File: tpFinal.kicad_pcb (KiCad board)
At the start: 2 copper layers, 50 x 100 mm, 42 parts, among them P1 CONN_UART_TX_RX, P2 CONN_SPK, P3 CONN_PWR, P4 CONN_BAT, P5 CONN_SWD, U1 EMW3166, U2 MCP73831-2-OT, U3 AUR9705AGH, U4 SPH0644HM4H-1, U5 MAX98357A

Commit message: correciones varias según revisiones
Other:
- board text added: "Fabricante: seeedstudio Grillas: 1 mm ,0,5 mm , 0,25 mm Via: 0.8 mm / 0.4 mm Margen: 0.2 mm Pista: 0.6 mm, 0.4 mm, 0,25 mm , 0.2 mm Dist. a borde: 0.80 mm Material: FR-4 TG130 Terminacion: HASL"
- board text removed: "Grillas: 1 mm ,0,5 mm , 0,25 mm Via: 0.8 mm / 0.4 mm Margen: 0.2 mm Pista: 0.6 mm, 0.4 mm, 0,25 mm , 0.2 mm Dist. a borde: 0.80 mm Material: FR-4 TG130 Terminacion: HASL"
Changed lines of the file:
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@@
     (tags resistor)
     (attr smd)
-    (fp_text reference R5 (at 0 -1.65 270) (layer F.SilkS)
+    (fp_text reference R5 (at 2.4375 -0.5) (layer F.SilkS)
       (effects (font (size 1 1) (thickness 0.15)))
     )
@@
     (tags resistor)
     (attr smd)
-    (fp_text reference R6 (at 0 -1.65 270) (layer F.SilkS)
+    (fp_text reference R6 (at 2.4375 -0.5) (layer F.SilkS)
       (effects (font (size 1 1) (thickness 0.15)))
     )
@@
     (tags resistor)
     (attr smd)
-    (fp_text reference R7 (at 0 -1.65 270) (layer F.SilkS)
+    (fp_text reference R7 (at 2.9375 -0.5) (layer F.SilkS)
       (effects (font (size 1 1) (thickness 0.15)))
     )
@@
     (tags resistor)
     (attr smd)
-    (fp_text reference R8 (at 0 -1.65 270) (layer F.SilkS)
+    (fp_text reference R8 (at 2.9375 -0.5 180) (layer F.SilkS)
       (effects (font (size 1 1) (thickness 0.15)))
     )
@@
       (solder_mask_margin 0.5) (clearance 0.5))
   )
-  (gr_text "Grillas: 1 mm ,0,5 mm , 0,25 mm\nVia: 0.8 mm / 0.4 mm\nMargen: 0.2 mm\nPista: 0.6 mm, 0.4 mm, 0,25 mm , 0.2 mm\nDist. a borde: 0.80 mm\nMaterial: FR-4 TG130\nTerminacion: HASL" (at 198 61) (layer Dwgs.User)
+  (gr_text "Fabricante: seeedstudio\nGrillas: 1 mm ,0,5 mm , 0,25 mm\nVia: 0.8 mm / 0.4 mm\nMargen: 0.2 mm\nPista: 0.6 mm, 0.4 mm, 0,25 mm , 0.2 mm\nDist. a borde: 0.80 mm\nMaterial: FR-4 TG130\nTerminacion: HASL" (at 198 61) (layer Dwgs.User)
     (effects (font (size 1.5 1.5) (thickness 0.3)) (justify left))
   )
@@
     (effects (font (size 1.5 1.5) (thickness 0.3)) (justify mirror))
   )
-  (dimension 94 (width 0.3) (layer F.SilkS)
-    (gr_text "94,000 mm" (at 192.1 88 270) (layer F.SilkS)
+  (dimension 94 (width 0.3) (layer Dwgs.User)
+    (gr_text "94,000 mm" (at 192.1 88 270) (layer Dwgs.User)
       (effects (font (size 1.5 1.5) (thickness 0.3)))
     )
@@
     (arrow2b (pts (xy 190 41) (xy 190.586421 42.126504)))
   )
-  (dimension 44 (width 0.3) (layer F.SilkS)
-    (gr_text "44,000 mm" (at 162 142.1) (layer F.SilkS)
+  (dimension 44 (width 0.3) (layer Dwgs.User)
+    (gr_text "44,000 mm" (at 162 142.1) (layer Dwgs.User)
       (effects (font (size 1.5 1.5) (thickness 0.3)))
     )
@@
     (arrow2b (pts (xy 140 140) (xy 141.126504 139.413579)))
   )
-  (dimension 100 (width 0.3) (layer F.SilkS)
-    (gr_text "100,000 mm" (at 196.1 88 270) (layer F.SilkS)
+  (dimension 100 (width 0.3) (layer Dwgs.User)
+    (gr_text "100,000 mm" (at 196.1 88 270) (layer Dwgs.User)
       (effects (font (size 1.5 1.5) (thickness 0.3)))
     )
@@
     (arrow2b (pts (xy 194 38) (xy 194.586421 39.126504)))
   )
-  (dimension 50 (width 0.3) (layer F.SilkS)
-    (gr_text "50,000 mm" (at 162 146.1) (layer F.SilkS)
+  (dimension 50 (width 0.3) (layer Dwgs.User)
+    (gr_text "50,000 mm" (at 162 146.1) (layer Dwgs.User)
       (effects (font (size 1.5 1.5) (thickness 0.3)))
     )

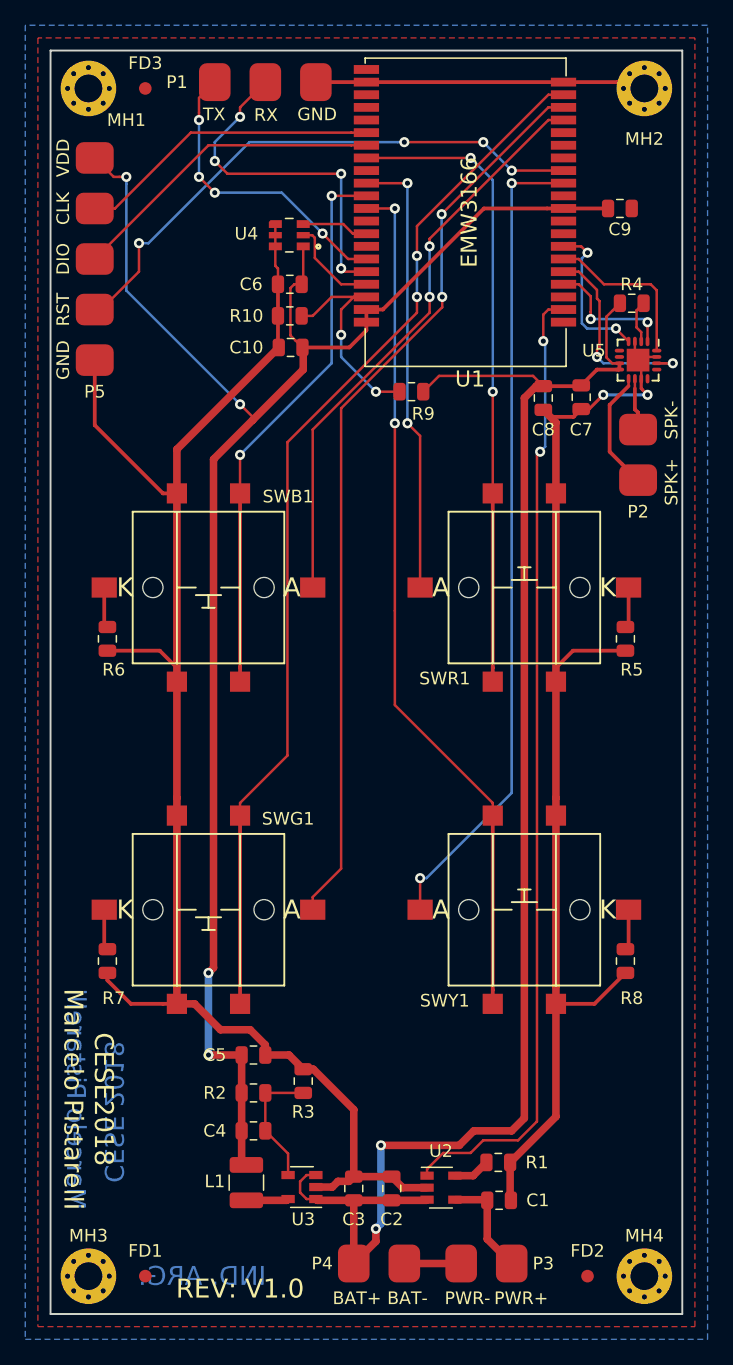
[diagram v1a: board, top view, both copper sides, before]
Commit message: Referencias de fiduciales y agujeros de sujeción configuradas invisibles
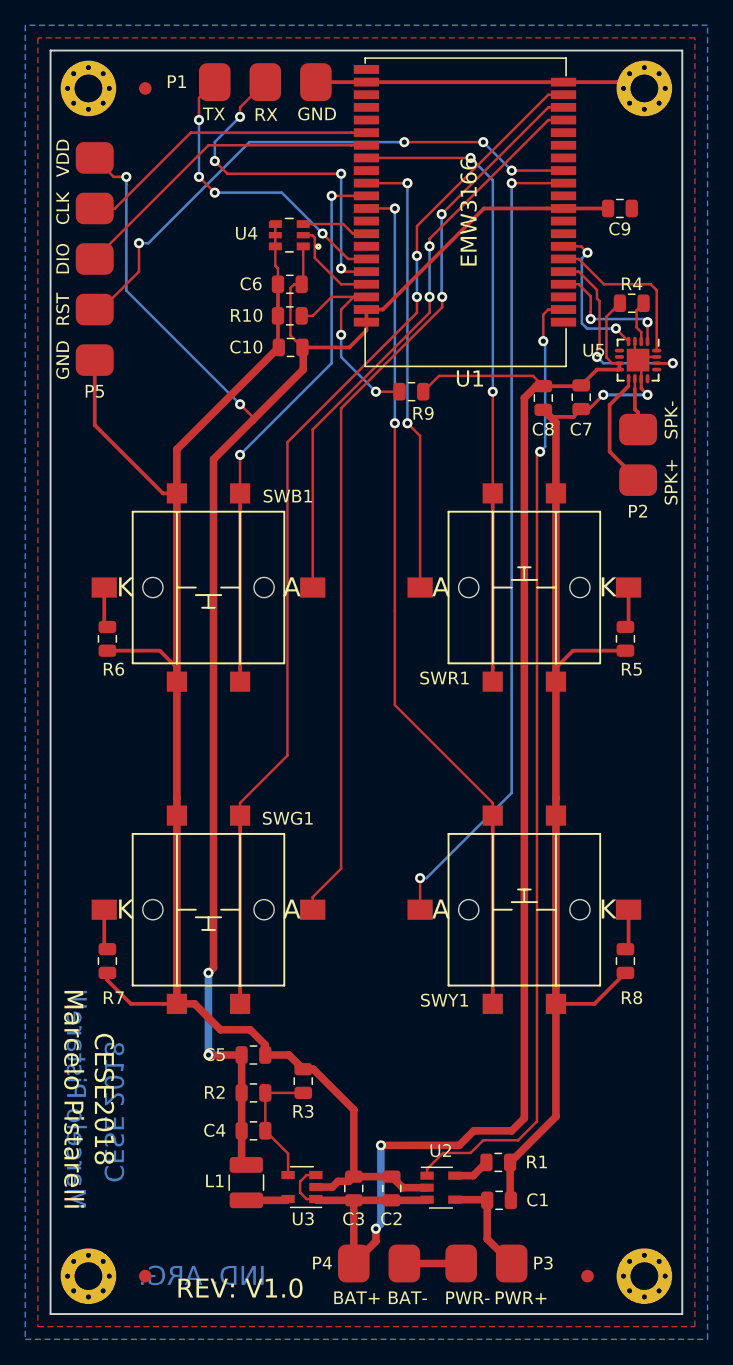
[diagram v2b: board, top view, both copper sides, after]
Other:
- board text added: "Reglas de fabricación de SeeedStudio: 1) https://www.seeedstudio.com/fusion_pcb.html 2) http://support.seeedstudio.com/knowledgebase/articles/447362-fusion-pcb-specification El criterio de selección de ancho mínimo de pista de 6/6 mil es conforme a las capacidades de fabricación de SeeedStudio. Donde 6/6 mil es la tecnología más económica que ofrece, también soporta a un mayor precio las tecnolog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"
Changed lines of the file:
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@@
-(kicad_pcb (version 20171130) (host pcbnew 5.0.0-fee4fd1~66~ubuntu16.04.1)
+(kicad_pcb (version 20171130) (host pcbnew 5.0.1-33cea8e~67~ubuntu16.04.1)
   (general
     (thickness 1.6)
-    (drawings 14)
+    (drawings 15)
     (tracks 398)
     (zones 0)
@@
     (date 2018-10-18)
     (rev 1.0)
-    (company "Marcelo Pistarelli")
+    (company "Empresa: Marcelo Pistarelli")
+    (comment 1 "Creative Commons - Attribution - ShareAlike 3.0")
   )
   (layers
@@
     (pad_drill 0.762)
     (pad_to_mask_clearance 0.2)
+    (solder_mask_min_width 0.25)
     (aux_axis_origin 0 0)
     (visible_elements FFFFFF7F)
@@
     (tags "mounting hole 2.2mm m2")
     (attr virtual)
-    (fp_text reference MH1 (at 3 2.5) (layer F.SilkS)
+    (fp_text reference MH1 (at 3 2.5) (layer F.SilkS) hide
       (effects (font (size 1 1) (thickness 0.15)))
     )
@@
     (tags "mounting hole 2.2mm m2")
     (attr virtual)
-    (fp_text reference MH2 (at 0 4) (layer F.SilkS)
+    (fp_text reference MH2 (at 0 4) (layer F.SilkS) hide
       (effects (font (size 1 1) (thickness 0.15)))
     )
@@
     (tags "mounting hole 2.2mm m2")
     (attr virtual)
-    (fp_text reference MH3 (at 0 -3.2) (layer F.SilkS)
+    (fp_text reference MH3 (at 0 -3.2) (layer F.SilkS) hide
       (effects (font (size 1 1) (thickness 0.15)))
     )
@@
     (tags "mounting hole 2.2mm m2")
     (attr virtual)
-    (fp_text reference MH4 (at 0 -3.2) (layer F.SilkS)
+    (fp_text reference MH4 (at 0 -3.2) (layer F.SilkS) hide
       (effects (font (size 1 1) (thickness 0.15)))
     )
@@
     (tags marker)
     (attr virtual)
-    (fp_text reference FD1 (at 0 -2) (layer F.SilkS)
+    (fp_text reference FD1 (at 0 -2) (layer F.SilkS) hide
       (effects (font (size 1 1) (thickness 0.15)))
     )
@@
     (tags marker)
     (attr virtual)
-    (fp_text reference FD2 (at 0 -2) (layer F.SilkS)
+    (fp_text reference FD2 (at 0 -2) (layer F.SilkS) hide
       (effects (font (size 1 1) (thickness 0.15)))
     )
@@
     (tags marker)
     (attr virtual)
-    (fp_text reference FD3 (at 0 -2) (layer F.SilkS)
+    (fp_text reference FD3 (at 0 -2) (layer F.SilkS) hide
       (effects (font (size 1 1) (thickness 0.15)))
     )
@@
       (solder_mask_margin 0.5) (clearance 0.5))
   )
+  (gr_text "Reglas de fabricación de SeeedStudio:\n\n1) https://www.seeedstudio.com/fusion_pcb.html\n2) http://support.seeedstudio.com/knowledgebase/articles/447362-fusion-pcb-specification\n\n\nEl criterio de selección de ancho mínimo de pista de 6/6 mil es conforme a las capacidades de fabricación de SeeedStudio. \nDonde 6/6 mil es la tecnología más económica que ofrece, también soporta a un mayor precio las tecnologías de 5/5 mil y 4/4 mil.\n\nYa se han fabricado en SeeedStudio varias placas con tecnología 6/6 mil sin fallas." (at 95 160) (layer Dwgs.User)
+    (effects (font (size 1.5 1.5) (thickness 0.3)))
+  )
   (gr_text "Fabricante: seeedstudio\nGrillas: 1 mm ,0,5 mm , 0,25 mm\nVia: 0.8 mm / 0.4 mm\nMargen: 0.2 mm\nPista: 0.6 mm, 0.4 mm, 0,25 mm , 0.2 mm\nDist. a borde: 0.80 mm\nMaterial: FR-4 TG130\nTerminacion: HASL" (at 198 61) (layer Dwgs.User)
